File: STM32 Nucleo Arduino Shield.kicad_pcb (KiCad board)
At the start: 2 copper layers, 68.6 x 53.3 mm, 8 parts, among them P1 Power, P2 Analog, P3 Digital, P4 Digital, P5 CONN_1, P6 CONN_1, P7 CONN_1, P8 CONN_1

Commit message: footprints assigned, netlist generated, layout started
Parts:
- added C1: 100n, MyModules:SM0603-C-JRL, F.Cu at (149.2, 82.9)
- added C10, C11, C12, C13, C14, C15, C16, C17, C18, C19, C20, C21: 100n, MyModules:SM0603-C-JRL, F.Cu at (145.3, 136.4)
- added C2: 100p, MyModules:SM0603-C-JRL, F.Cu at (137.0, 87.4)
- added C22, C23: 22μF, MyModules:jrl_c_elec_5x5.3, F.Cu at (145.3, 136.4)
- added C24, C25, C26, C27, C28, C29, C30, C31, C32, C33, C34, C35, C36, C37, C38, C39: 0.01µ, MyModules:SM0603-C-JRL, F.Cu at (145.3, 136.4)
- added C3: 100n, MyModules:SM0603-C-JRL, F.Cu at (143.2, 87.2)
- added C4: 1μ, MyModules:SM0603-C-JRL, F.Cu at (138.0, 89.9)
- added C40: 0.1µ, MyModules:SM0603-C-JRL, F.Cu at (145.3, 136.4)
- added C5: 4.7μ, MyModules:SM0805-HAND, F.Cu at (145.2, 87.6)
- added C6, C7, C8, C9: 22p, MyModules:SM0603-C-JRL, F.Cu at (145.3, 136.4)
- added D1, D2, D3, D4: LED, MyModules:LED-0805-JRL, F.Cu at (145.3, 136.4)
- added D5, D6: S1BB, MyModules:SMB-1C2A, F.Cu at (145.3, 136.4)
- added D7: 1N4148, MyModules:SOD323-C1A2, F.Cu at (145.3, 136.4)
- added J1: PJ-301B, MyModules:PJ-301B-JACK-SLOTS, F.Cu at (162.5, 146.9)
- added J2: PJ-301B, MyModules:PJ-301B-JACK-SLOTS, F.Cu at (179.0, 147.1)
- added J3: PJ-301B, MyModules:PJ-301B-JACK-SLOTS, F.Cu at (193.5, 146.6)
- added OC1: 6N137, MyModules:8-SMD, F.Cu at (205.2, 104.4)
- added P10, P11, P12, P14, P15, P16, P17, P18, P19, P20, P21, P22, P23, P24, P25, P26, P27, P28, P29, P9: CONN_01X01, MyModules:TEST_POINT_5000_SERIES, F.Cu at (145.3, 136.4)
- added P13: CONN_02X05, Pin_Headers:Pin_Header_Straight_2x05_Pitch1.27mm, F.Cu at (164.7, 88.1)
- added R1, R2, R3, R4, R5, R6: 10K, MyModules:SM0603-R-JRL, F.Cu at (145.3, 136.4)
- added R10: 0, MyModules:SM0603-R-JRL, B.Cu at (131.0, 98.3)
- added R11, R12, R13, R29, R9: 1K, MyModules:SM0603-R-JRL, F.Cu at (145.3, 136.4)
- added R14: 1K, MyModules:SM0603-R-JRL, F.Cu at (138.7, 87.4)
- added R15: 22K, MyModules:SM0603-R-JRL, F.Cu at (151.7, 113.4)
- added R16: 22K, MyModules:SM0603-R-JRL, F.Cu at (138.2, 108.1)
- added R17: 47K, MyModules:SM0603-R-JRL, F.Cu at (127.2, 88.1)
- added R18: 47K, MyModules:SM0603-R-JRL, F.Cu at (125.2, 88.1)
- added R19: 68K, MyModules:SM0603-R-JRL, F.Cu at (153.7, 113.4)
- added R20: 68K, MyModules:SM0603-R-JRL, F.Cu at (144.5, 107.6)
- added R21: 220K, MyModules:SM0603-R-JRL, F.Cu at (131.2, 85.6)
- added R22: 220K, MyModules:SM0603-R-JRL, F.Cu at (120.7, 84.6)
- added R23: 1K, MyModules:SM0603-R-JRL, F.Cu at (133.2, 83.1)
- added R24: 1K, MyModules:SM0603-R-JRL, F.Cu at (120.7, 86.4)
- added R25: 4.7K, MyModules:SM0603-R-JRL, F.Cu at (145.3, 136.4)
- added R26, R27: 10, MyModules:SM0805-HAND, F.Cu at (145.3, 136.4)
- added R28: 220, MyModules:SM0603-R-JRL, F.Cu at (145.3, 136.4)
- added R7: 82k, MyModules:SM0603-R-JRL, F.Cu at (135.2, 87.4)
- added R8: 39K, MyModules:SM0603-R-JRL, F.Cu at (135.2, 90.4)
- added SW1: TACT_SWITCH, MyModules:B3F-1050-OMRON, F.Cu at (145.3, 136.4)
- added U1: OPA2171, Housings_SSOP:TSSOP-8_3x3mm_Pitch0.65mm, F.Cu at (165.7, 81.9)
- added U10, U11, U2, U3: TL074-, Housings_SSOP:TSSOP-14_4.4x5mm_Pitch0.65mm, F.Cu at (145.3, 136.4)
- added U12: OPA2171, Housings_SSOP:TSSOP-8_3x3mm_Pitch0.65mm, F.Cu at (126.2, 84.6)
- added U4: SN7407, Housings_SOIC:SOIC-14_3.9x8.7mm_Pitch1.27mm, F.Cu at (145.3, 136.4)
- added U5: LM1117, TO_SOT_Packages_SMD:SOT-223, F.Cu at (151.0, 92.4)
- added U6: TS321, TO_SOT_Packages_SMD:SOT-23-5, F.Cu at (132.0, 89.4)
- added U7: MAX5134, Housings_SSOP:TSSOP-16_4.4x5mm_Pitch0.65mm, F.Cu at (142.0, 82.6)
- added U8, U9: CD4051, MyModules:TSSOP-16_4.4x5mm_Pitch0.65mm_jrl, F.Cu at (145.3, 136.4)
- added VR1: 10K, MyModules:R0904N-SONG-HUEI, F.Cu at (119.0, 139.9)
- added VR2: 1K, MyModules:TC33X-2, F.Cu at (152.0, 109.4)
- added VR3: 1K, MyModules:TC33X-2, F.Cu at (141.2, 109.4)
- added X1: MIDI IN, MyModules:SD-50BV-5DIN, F.Cu at (199.7, 83.4)
- moved P3 22.9 mm to (152.7, 75.6), turned to 180 degrees
- moved P4 17.8 mm to (174.5, 75.6), turned to 180 degrees
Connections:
- net /1(Tx) renamed Net-(P4-Pad7)
- net /13(SCK) renamed Net-(P3-Pad5)
- net /3(**) renamed Net-(P4-Pad5)
- net /8 renamed Net-(P3-Pad10)
- net /9(**) renamed Net-(P3-Pad9)
- net /AREF renamed Net-(P3-Pad3)
- net /IOREF renamed Net-(P1-Pad2)
- net /Reset renamed Net-(P1-Pad3)
- net /Vin renamed Net-(P1-Pad8)
- P2 pad 1: /A0 -> /D0
- P2 pad 2: /A1 -> /D1
- P2 pad 3: /A2 -> /LED0
- P2 pad 4: /A3 -> /LED1
- P2 pad 5: /A4(SDA) -> Net-(P2-Pad5)
- P2 pad 6: /A5(SCL) -> /LED2
- P3 pad 1: /A5(SCL) -> /~LDAC
- P3 pad 2: /A4(SDA) -> Net-(P3-Pad2)
- P3 pad 4: GND -> /MOSI
- P3 pad 6: /12(MISO) -> /SCK
- P3 pad 7: /11(**/MOSI) -> GND
- P3 pad 8: /10(**/SS) -> /AVDD
- P4 pad 1: /7 -> /MIDI_RX
- P4 pad 2: /6(**) -> /D2
- P4 pad 3: /5(**) -> /LED3
- P4 pad 4: /4 -> /~DAC_MUX0
- P4 pad 6: /2 -> /~DAC_MUX1
- P4 pad 8: /0(Rx) -> /~DAC_SEL
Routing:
- net /~DAC_SEL: track 0.00 -> 19.7 mm, vias 0 -> 1
- net /~LDAC: track 0.00 -> 18.2 mm, vias 0 -> 1
- net Net-(U12-Pad5): track 0.00 -> 15.8 mm
- net /DAC_AVDD: track 0.00 -> 14.7 mm
- net Net-(U12-Pad3): track 0.00 -> 10.9 mm
- net Net-(U1-Pad3): track 0.00 -> 10.0 mm
- net /SCK: track 0.00 -> 9.31 mm
- net Net-(U1-Pad5): track 0.00 -> 9.27 mm
- net /REF0: track 0.00 -> 7.46 mm
- net /VREF: track 0.00 -> 5.88 mm
- net /MOSI: track 0.00 -> 4.81 mm
- net Net-(C8-Pad2): track 0.00 -> 3.92 mm
- net /VDAC1: track 0.00 -> 3.66 mm
- net Net-(C6-Pad2): track 0.00 -> 3.27 mm
- net Net-(R19-Pad1): track 0.00 -> 2.17 mm
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
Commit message: routing routing routing
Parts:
- moved J3 103.8 mm to (117.2, 76.1), turned to 180 degrees
- moved J2 81.5 mm to (117.5, 93.6)
- moved C8 57.0 mm to (119.8, 85.5), turned to 90 degrees
- moved C6 53.1 mm to (128.4, 86.1), turned to 90 degrees
- moved P13 52.6 mm to (115.0, 105.1)
- moved P10 52.3 mm to (133.0, 85.6)
- moved C9 49.2 mm to (161.3, 89.9), turned to 270 degrees
- moved C7 47.5 mm to (151.5, 89.3), turned to 270 degrees
- moved R1 44.0 mm to (174.0, 103.1), turned to 90 degrees
- moved U10 41.8 mm to (187.0, 133.9)
- moved U9 38.9 mm to (167.0, 104.1)
- moved U11 34.2 mm to (175.5, 152.4)
- moved U8 32.7 mm to (150.2, 104.1)
- moved U4 27.8 mm to (162.7, 114.9), turned to 180 degrees
- moved VR3 25.6 mm to (161.8, 94.2), turned to 0 degrees
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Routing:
- net /VDAC2: track 0.00 -> 20.6 mm
- net /VDAC1: track 3.66 -> 22.0 mm
- net /A: track 0.00 -> 17.0 mm
- net /LED0: track 0.00 -> 16.7 mm
- net /~DAC_MUX0_EN: track 0.00 -> 15.2 mm
- net /B: track 0.00 -> 13.1 mm
- net /~DAC_MUX1_EN: track 0.00 -> 12.7 mm
- net /D1: track 0.00 -> 10.7 mm
- net Net-(C7-Pad2): track 2.00 -> 12.5 mm
- net Net-(U1-Pad5): track 9.27 -> 19.6 mm
- net Net-(C9-Pad2): track 0.00 -> 10.3 mm
- net Net-(C8-Pad2): track 3.92 -> 13.6 mm
- net /C: track 0.00 -> 8.06 mm
- net /D0: track 0.00 -> 6.93 mm
- net Net-(U1-Pad3): track 10.0 -> 16.7 mm
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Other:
- board size 68.6 x 53.3 mm -> 75.7 x 55.2 mm
- net class Power added: clearance 0.2, trace_width 0.35, via_dia 0.8, via_drill 0.4

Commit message: more tedious routing
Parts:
- moved U4 4.00 mm to (158.7, 114.9)
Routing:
- net /C: track 8.06 -> 34.2 mm, vias 0 -> 2
- net /B: track 13.1 -> 37.4 mm, vias 0 -> 2
- net /A: track 17.0 -> 41.2 mm, vias 0 -> 2
- net /~DAC_MUX1_EN: track 12.7 -> 17.3 mm
- net /~DAC_MUX0_EN: track 15.2 -> 12.1 mm
- net /D0: track 6.93 -> 5.74 mm
- net /LED0: track 16.7 -> 17.6 mm
- net /D1: track 10.7 -> 9.81 mm

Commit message: mostly routed S&H circuits
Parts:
- P10, P11, P12, P14, P15, P16, P17, P18, P19, P20, P21, P22, P23, P24, P25, P26, P27, P28, P29, P9: footprint MyModules:TEST_POINT_5000_SERIES -> MyModules:TEST_POINT_SMALL
- R1, R2, R3, R4, R5: moved to B.Cu
- moved P13 76.0 mm to (191.0, 104.9)
- moved SW1 68.9 mm to (155.2, 80.9)
- moved J1 60.9 mm to (117.5, 105.9)
- moved C40 59.2 mm to (162.0, 79.6), turned to 90 degrees
- moved R25 57.6 mm to (160.2, 80.9), turned to 90 degrees
- moved R29 56.4 mm to (162.0, 82.6), turned to 90 degrees
- moved U11 53.2 mm to (153.0, 104.1)
- moved R28 53.0 mm to (172.0, 90.6)
- moved D7 51.5 mm to (168.2, 90.4), turned to 180 degrees
- moved R5 46.5 mm to (182.0, 107.9), turned to 270 degrees
- moved R4 44.8 mm to (179.7, 107.9), turned to 270 degrees
- moved R3 43.4 mm to (178.0, 107.9), turned to 270 degrees
- moved P8 42.9 mm to (199.5, 127.4)
- moved OC1 42.5 mm to (168.2, 83.4)
- moved R2 42.1 mm to (176.0, 107.6), turned to 270 degrees
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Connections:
- C24 pad 1: /CV0 -> /CV2
- C26 pad 1: /CV2 -> /CV0
- C29 pad 1: /CV5 -> /CV6
- C30 pad 1: /CV6 -> /CV7
- C31 pad 1: /CV7 -> /CV5
- C32 pad 1: /CV8 -> /CV10
- C34 pad 1: /CV10 -> /CV8
- C37 pad 1: /CV13 -> /CV14
- C38 pad 1: /CV14 -> /CV13
- U10 pad 10: /CV10 -> /CV8
- U10 pad 3: /CV8 -> /CV10
- U11 pad 10: /CV14 -> /CV13
- U11 pad 5: /CV13 -> /CV14
- U2 pad 10: /CV2 -> /CV0
- U2 pad 3: /CV0 -> /CV2
- U3 pad 10: /CV6 -> /CV7
- U3 pad 12: /CV7 -> /CV5
- U3 pad 5: /CV5 -> /CV6
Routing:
- net /A: track 41.2 -> 1.70 mm, vias 2 -> 1
- net /B: track 37.4 -> 0.45 mm, vias 2 -> 0
- net /C: track 34.2 -> 0.49 mm, vias 2 -> 0
- net /MIDI_RX: track 0.00 -> 21.7 mm
- net /CV1: track 0.00 -> 20.5 mm
- net /CV0: track 0.00 -> 20.1 mm
- net /CV6: track 0.00 -> 19.3 mm
- net /CV2: track 0.00 -> 18.8 mm
- net /CV4: track 0.00 -> 17.8 mm
- net /CV7: track 0.00 -> 17.3 mm
- net /CV9: track 0.00 -> 17.0 mm
- net /CV3: track 0.00 -> 17.0 mm
- net /CV14: track 0.00 -> 16.5 mm
- net /CV8: track 0.00 -> 16.2 mm
- net /CV12: track 0.00 -> 16.1 mm
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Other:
- outline, holes or cut-outs redrawn

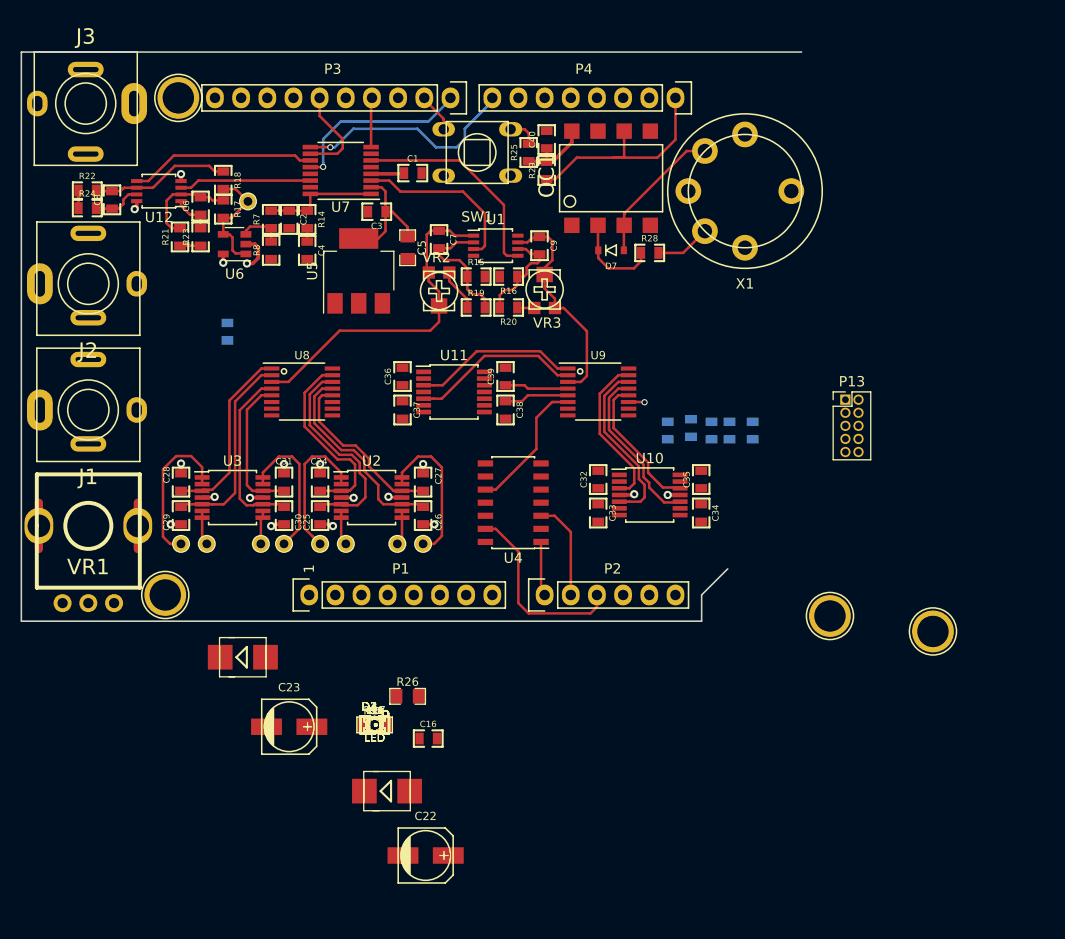
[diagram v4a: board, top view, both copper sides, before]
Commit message: everything placed and routing. stitching ground
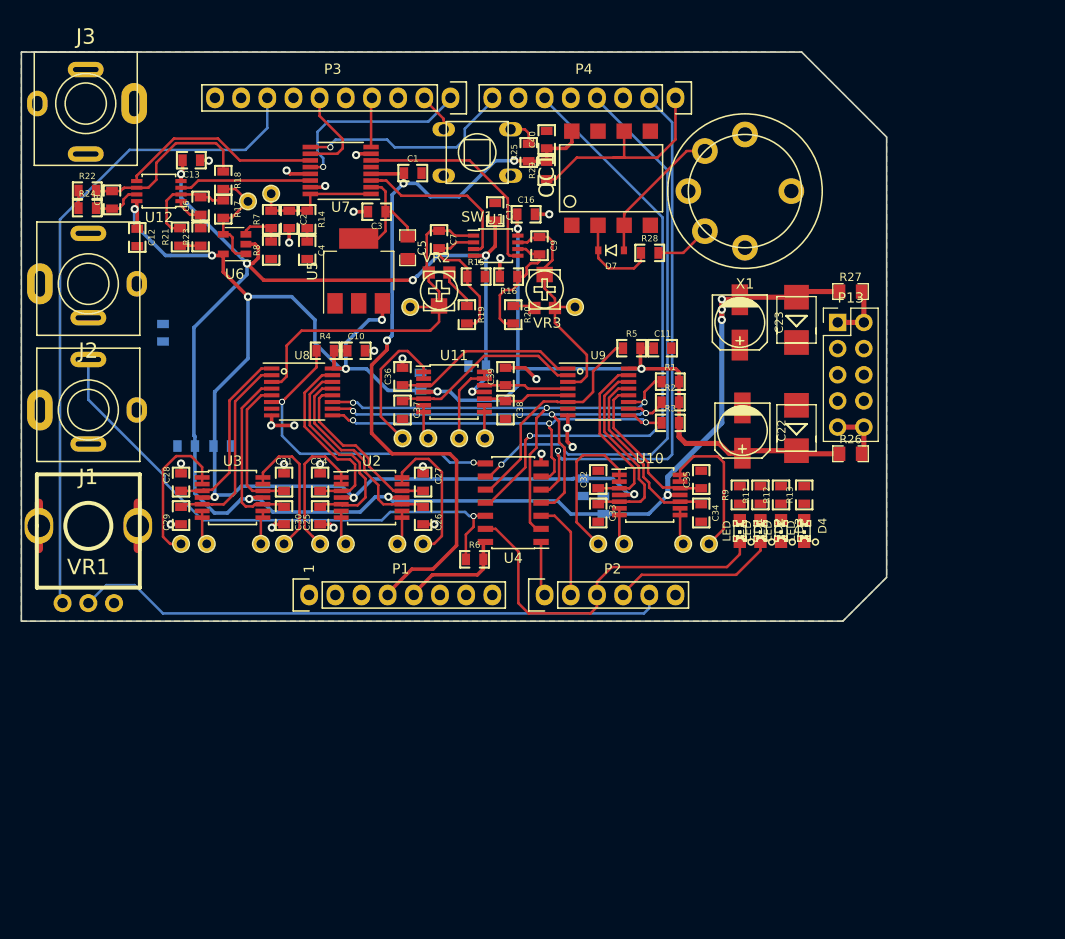
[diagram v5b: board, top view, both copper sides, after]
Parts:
- removed P5, P6, P7, P8: CONN_1, Socket_Arduino_Uno:Arduino_1pin
- C14, C15, C18, C19, C20, C21: moved to B.Cu
- P13: footprint Pin_Headers:Pin_Header_Straight_2x05_Pitch1.27mm -> Pin_Headers:Pin_Header_Straight_2x05_Pitch2.54mm
- R1, R2, R3, R4, R5: moved to F.Cu
- moved D6 62.9 mm to (186.2, 97.1), turned to 90 degrees
- moved R27 62.5 mm to (191.5, 94.4)
- moved C23 58.8 mm to (180.7, 97.4), turned to 270 degrees
- moved C13 57.6 mm to (127.5, 81.6), turned to 180 degrees
- moved D5 53.1 mm to (186.2, 107.6), turned to 90 degrees
- moved C12 52.6 mm to (122.2, 89.1), turned to 270 degrees
- moved P9 52.5 mm to (135.2, 84.9)
- moved C16 51.8 mm to (160.0, 86.9)
- moved C22 51.5 mm to (181.0, 107.9), turned to 270 degrees
- moved C17 51.2 mm to (157.0, 86.6), turned to 270 degrees
- moved R26 49.0 mm to (191.5, 110.1)
- moved R13 47.3 mm to (187.0, 114.1), turned to 90 degrees
- moved C11 46.0 mm to (173.2, 99.9)
- moved D4 45.8 mm to (187.0, 117.6), turned to 270 degrees
- moved R12 45.3 mm to (184.7, 114.1), turned to 90 degrees
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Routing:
- net +12V: track 5.65 -> 194.4 mm, vias 5 -> 11
- net -12V: track 8.16 -> 175.1 mm, vias 5 -> 11
- net +3V3: track 10.6 -> 77.2 mm, vias 0 -> 3
- net /AVDD: track 0.00 -> 64.1 mm
- net /~DAC_MUX1: track 0.00 -> 58.2 mm, vias 0 -> 1
- net Net-(P2-Pad5): track 0.00 -> 57.8 mm
- net /~DAC_MUX0: track 0.00 -> 56.1 mm, vias 0 -> 1
- net /D2: track 0.00 -> 53.3 mm, vias 0 -> 1
- net /GATE_1: track 0.00 -> 52.7 mm, vias 0 -> 1
- net /A: track 1.70 -> 48.7 mm, vias 1 -> 3
- net /B: track 0.45 -> 45.4 mm, vias 0 -> 3
- net /C: track 0.49 -> 41.0 mm, vias 0 -> 3
- net /~DAC_MUX0_EN: track 0.00 -> 31.5 mm, vias 0 -> 2
- net GND: track 8.38 -> 33.4 mm, vias 8 -> 24
- net /LED0: track 19.0 -> 36.5 mm
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- added copper zone on B.Cu, net GND
- added copper zone on F.Cu, net GND
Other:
- board size 75.7 x 55.2 mm -> 84 x 55.2 mm

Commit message: routed. weird Socket_Arduino_Uno library glitch required reinstalling footprint library from Arduino tempalte folder
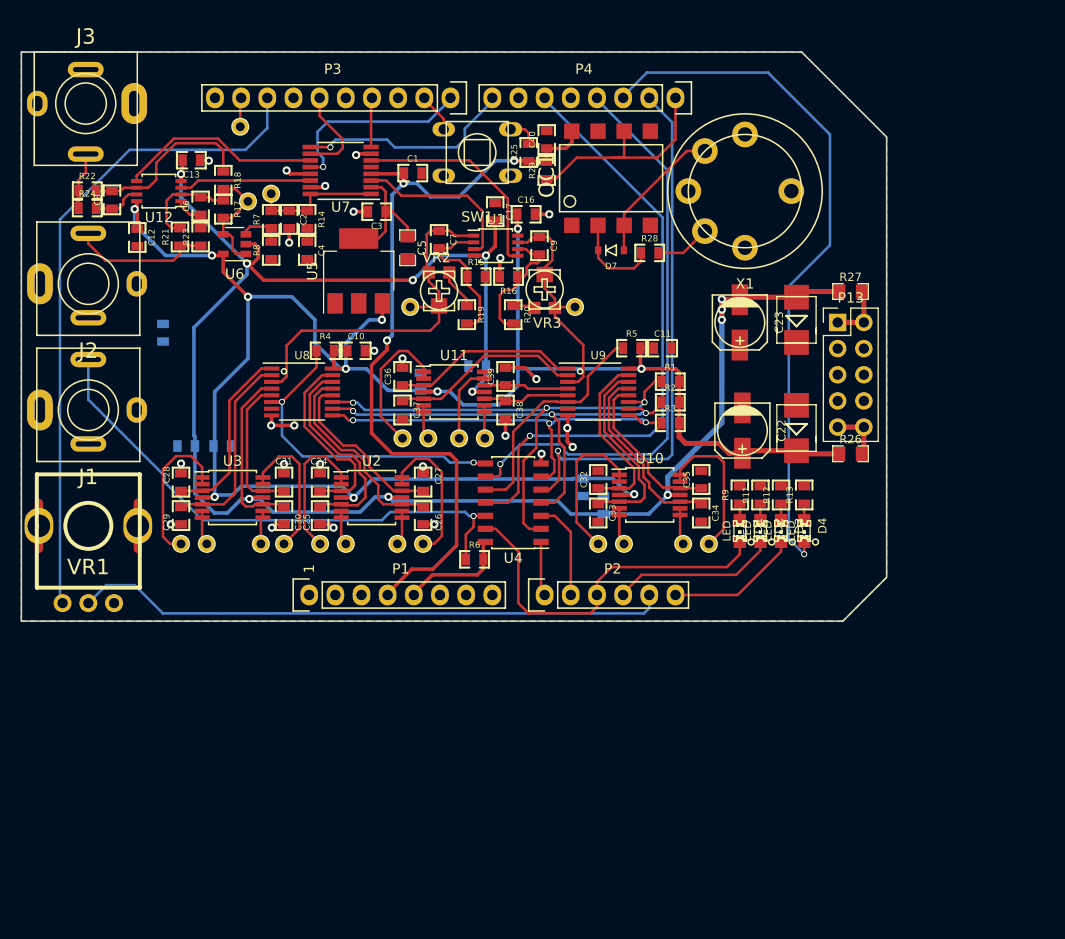
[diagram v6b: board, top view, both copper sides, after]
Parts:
- added P30: CONN_01X01, MyModules:TEST_POINT_SMALL, F.Cu at (132.2, 78.4)
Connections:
- P3 pad 9: Net-(P3-Pad9) -> /ANALOG_IN
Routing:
- net /LED3: track 0.00 -> 67.9 mm, vias 0 -> 1
- net /LED2: track 0.00 -> 12.9 mm
- net Net-(J2-Pad3): track 2.00 -> 13.7 mm
- net Net-(J3-Pad3): track 1.70 -> 5.54 mm
- net /ANALOG_IN: track 0.00 -> 2.84 mm
- net GND: track 33.4 -> 35.1 mm, vias 24 -> 25
- net Net-(D4-Pad1): track 0.00 -> 1.60 mm
- net Net-(D3-Pad1): track 0.00 -> 1.60 mm
- net Net-(D2-Pad1): track 0.00 -> 1.60 mm
- net Net-(D1-Pad1): track 0.00 -> 1.60 mm
- net /A: track 48.7 -> 49.8 mm
- net /~DAC_MUX1: track 58.2 -> 59.3 mm
- net /~DAC_MUX1_EN: track 22.2 -> 23.0 mm
- net /~DAC_MUX0: track 56.1 -> 56.7 mm

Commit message: ready for checking
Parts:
- moved C2 1.75 mm to (138.7, 87.4)
- moved C4 1.75 mm to (137.0, 90.4)
- moved R14 1.75 mm to (137.0, 87.4)
- moved C12 1.50 mm to (123.7, 89.1)
- moved U5 0.56 mm to (143.2, 92.1)
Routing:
- net GND: track 35.1 -> 49.2 mm, vias 25 -> 28
- net /DAC_AVDD: track 12.4 -> 18.7 mm
- net -12V: track 175.1 -> 179.6 mm
- net +12V: track 194.7 -> 198.9 mm
- net /LED3: track 67.9 -> 63.8 mm
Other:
- board text added: "+3.3V"
- board text added: "+5V"
- board text added: "CV0"
- board text added: "CV1"
- board text added: "CV10"
- board text added: "CV11"
- board text added: "CV12"
- board text added: "CV13"
- board text added: "CV14"
- board text added: "CV15"
- board text added: "CV2"
- board text added: "CV3"
- board text added: "CV4"
- board text added: "CV5"
- board text added: "CV6"
- board text added: "CV7"
- board text added: "CV8"
- board text added: "CV9"
- board text added: "GATE"
- board text added: "GPIO_PB9"
- board text added: "OUT1"
- board text added: "OUT2"
- board text added: "VDAC1"
- board text added: "VDAC2"

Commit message: finished adding 3D models
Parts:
- added P31: CONN_01X01, MyModules:TEST_POINT_LOOP_4592, F.Cu at (130.2, 99.6)
- U6: value TS321 -> OPA171
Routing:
- net GND: track 49.2 -> 51.5 mm, vias 28 -> 29
- net /D2: track 53.3 -> 51.9 mm
- net -12V: track 179.6 -> 178.9 mm
- net /~DAC_MUX0: track 56.7 -> 56.2 mm
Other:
- board text added: "MOSI"
- board text added: "SCK"
